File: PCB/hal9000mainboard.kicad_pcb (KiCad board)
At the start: 2 copper layers, 40 x 60 mm, 23 parts, among them J1001 Conn_01x02, J1002 Conn_01x04, J1003 Conn_01x02, J1004 Conn_01x02, J1005 Conn_01x03, J1006 Conn_01x08, U1001 DFR0299, U1002 MOUDLE-SEEEDUINO-XIAO-ESP32C3

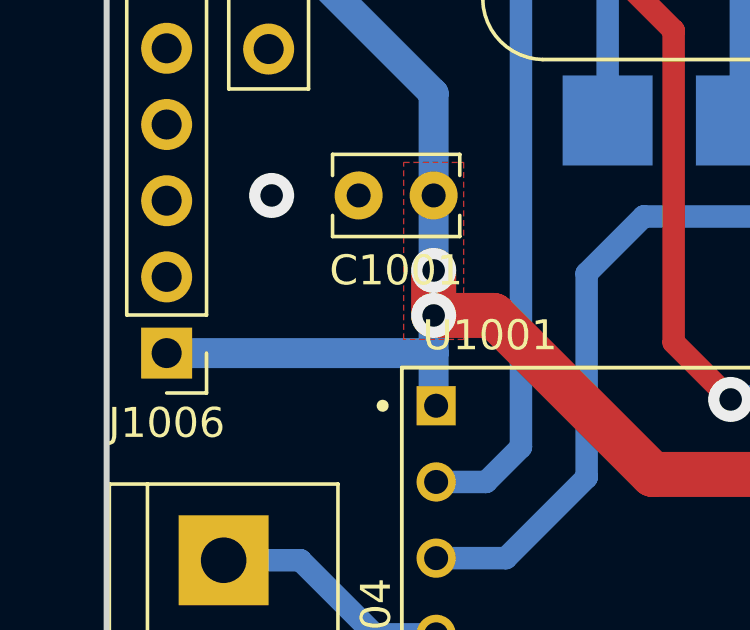
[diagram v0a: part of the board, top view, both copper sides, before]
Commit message: adxl345 fix, renaming, and song playing
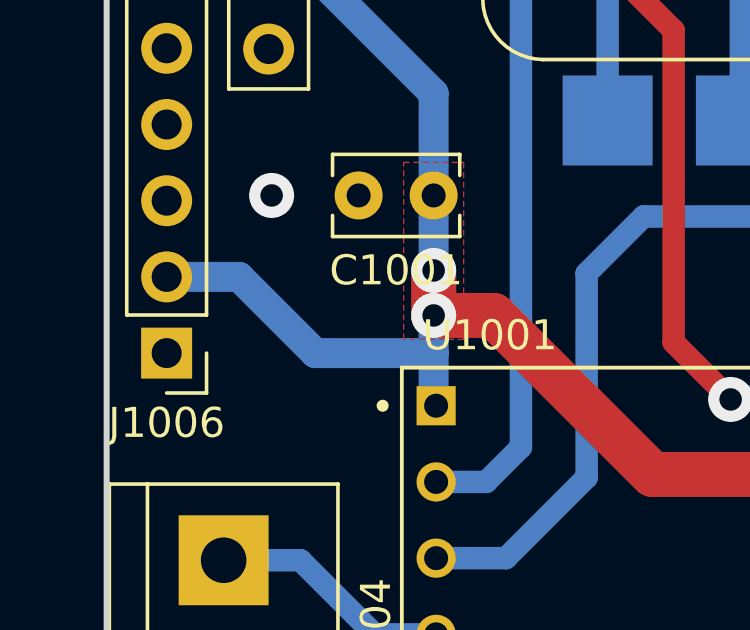
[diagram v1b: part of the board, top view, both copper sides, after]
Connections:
- J1006 pad 1: +5V -> GND
- J1006 pad 2: GND -> +5V
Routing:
- net +5V: track 86.9 -> 88.0 mm
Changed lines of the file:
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@@
 		(tags "C Rect series Radial pin pitch 2.50mm  length 4mm width 2.5mm Capacitor")
 		(property "Reference" "C1"
-			(at 1.25 -2.5 360)
+			(at 1.25 -2.5 0)
 			(layer "F.SilkS")
 			(effects
@@
 		)
 		(property "Value" "22uF x 25V X7R 1210"
-			(at 1.25 2.5 360)
+			(at 1.25 2.5 0)
 			(layer "F.Fab")
 			(effects
@@
 		)
 		(fp_text user "${REFERENCE}"
-			(at 1.25 0 360)
+			(at 1.25 0 0)
 			(layer "F.Fab")
 			(effects
@@
 			(layers "*.Cu" "*.Mask")
 			(remove_unused_layers no)
-			(net 2 "+5V")
+			(net 1 "GND")
 			(pinfunction "Pin_1")
 			(pintype "passive")
@@
 			(layers "*.Cu" "*.Mask")
 			(remove_unused_layers no)
-			(net 1 "GND")
+			(net 2 "+5V")
 			(pinfunction "Pin_2")
 			(pintype "passive")
@@
 		(tags "resistor")
 		(property "Reference" "R1003"
-			(at 0 1.43 360)
+			(at 0 1.43 0)
 			(layer "B.SilkS")
 			(effects
@@
 		)
 		(property "Value" "100"
-			(at 0 -1.43 360)
+			(at 0 -1.43 0)
 			(layer "B.Fab")
 			(effects
@@
 		)
 		(fp_text user "${REFERENCE}"
-			(at 0 0 360)
+			(at 0 0 0)
 			(layer "B.Fab")
 			(effects
@@
 	)
 	(segment
+		(start 6.955 35.355)
+		(end 10.9 35.355)
+		(width 1)
+		(layer "B.Cu")
+		(net 2)
+	)
+	(segment
+		(start 2 32.815)
+		(end 4.415 32.815)
+		(width 1)
+		(layer "B.Cu")
+		(net 2)
+	)
+	(segment
 		(start 35.14 34.54)
 		(end 33.2 32.6)
@@
 	)
 	(segment
+		(start 4.415 32.815)
+		(end 6.955 35.355)
+		(width 1)
+		(layer "B.Cu")
+		(net 2)
+	)
+	(segment
 		(start 10.9 33.683)
 		(end 10.9 37.027)
@@
 		(layer "B.Cu")
 		(net 2)
-	)
-	(segment
-		(start 2 35.355)
-		(end 10.9 35.355)
-		(width 1)
-		(layer "B.Cu")
-		(net 2)
